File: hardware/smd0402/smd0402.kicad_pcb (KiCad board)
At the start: 2 copper layers, 140 x 40 mm, 79 parts, among them J1 Conn_01x03, J2 Conn_01x03, T1 TestPoint_THTPad_3.0x3.0mm_Dr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, T12 TestPoint_THTPad_3.0x3.0mm_Dr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, T13 TestPoint_THTPad_3.0x3.0mm_Dr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, T14 TestPoint_THTPad_3.0x3.0mm_Dr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, T15 TestPoint_THTPad_3.0x3.0mm_Dr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, T16 TestPoint_THTPad_3.0x3.0mm_Dr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, T18 TestPoint_THTPad_3.0x3.0mm_Dr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, T19 TestPoint_THTPad_3.0x3.0mm_Dr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, T20 TestPoint_THTPad_3.0x3.0mm_Dr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, T21 TestPoint_THTPad_3.0x3.0mm_Dr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, T22 TestPoint_THTPad_3.0x3.0mm_Dr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, T42 TestPoint_THTPad_D1.0mm_Drill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, T43 TestPoint_THTPad_D1.0mm_Drill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, T44 TestPoint_THTPad_D1.0mm_Drill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, T45 TestPoint_THTPad_D1.0mm_Drill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, T46 TestPoint_THTPad_D1.0mm_Drill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, T48 TestPoint_THTPad_D1.0mm_Drill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, T49 TestPoint_THTPad_D1.0mm_Drill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, T50 TestPoint_THTPad_D1.0mm_Drill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, T51 TestPoint_THTPad_D1.0mm_Drill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, T51 TestPoint_THTPad_D2.0mm_Drill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, T52 TestPoint_THTPad_D1.0mm_Drill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, T52 TestPoint_THTPad_D2.0mm_Drill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, T53 TestPoint_THTPad_D2.0mm_Drill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, T54 TestPoint_THTPad_D2.0mm_Drill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, T55 TestPoint_THTPad_D2.0mm_Drill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, T56 TestPoint_THTPad_D2.0mm_Drill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, U1 WCH CH32V003F4U6

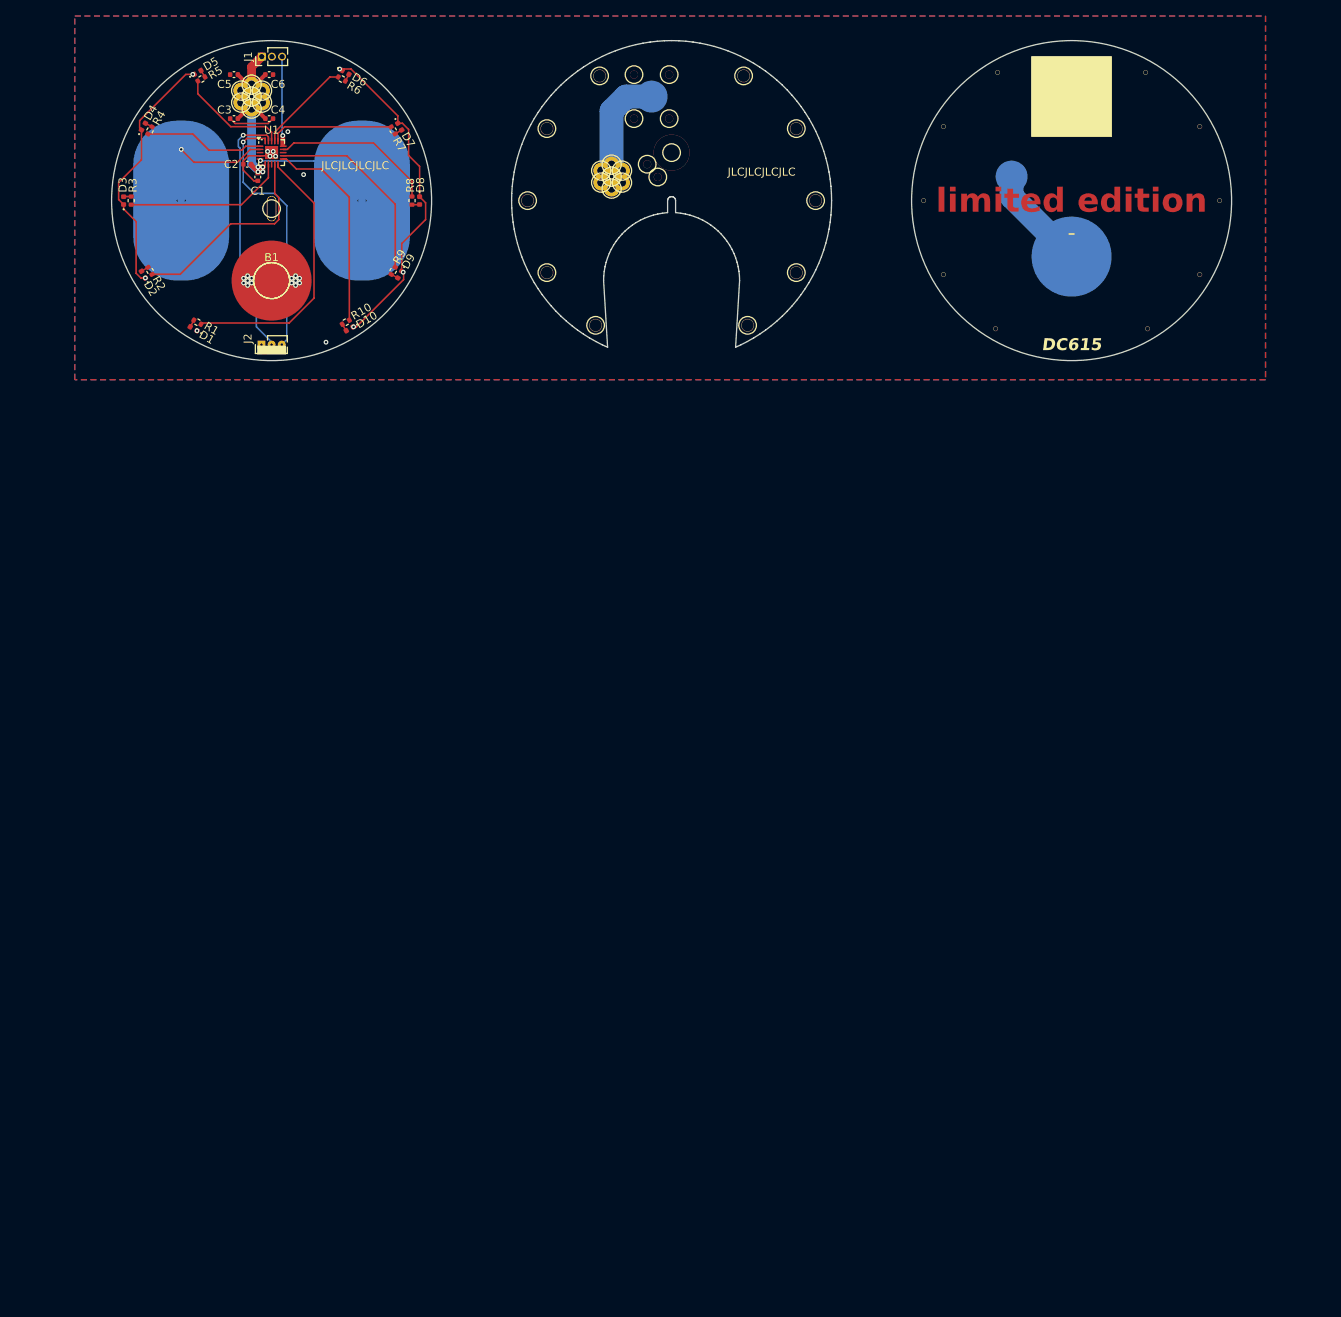
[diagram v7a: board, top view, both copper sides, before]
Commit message: boost dia to 50mm, use back-to-back LEDs, add SAO
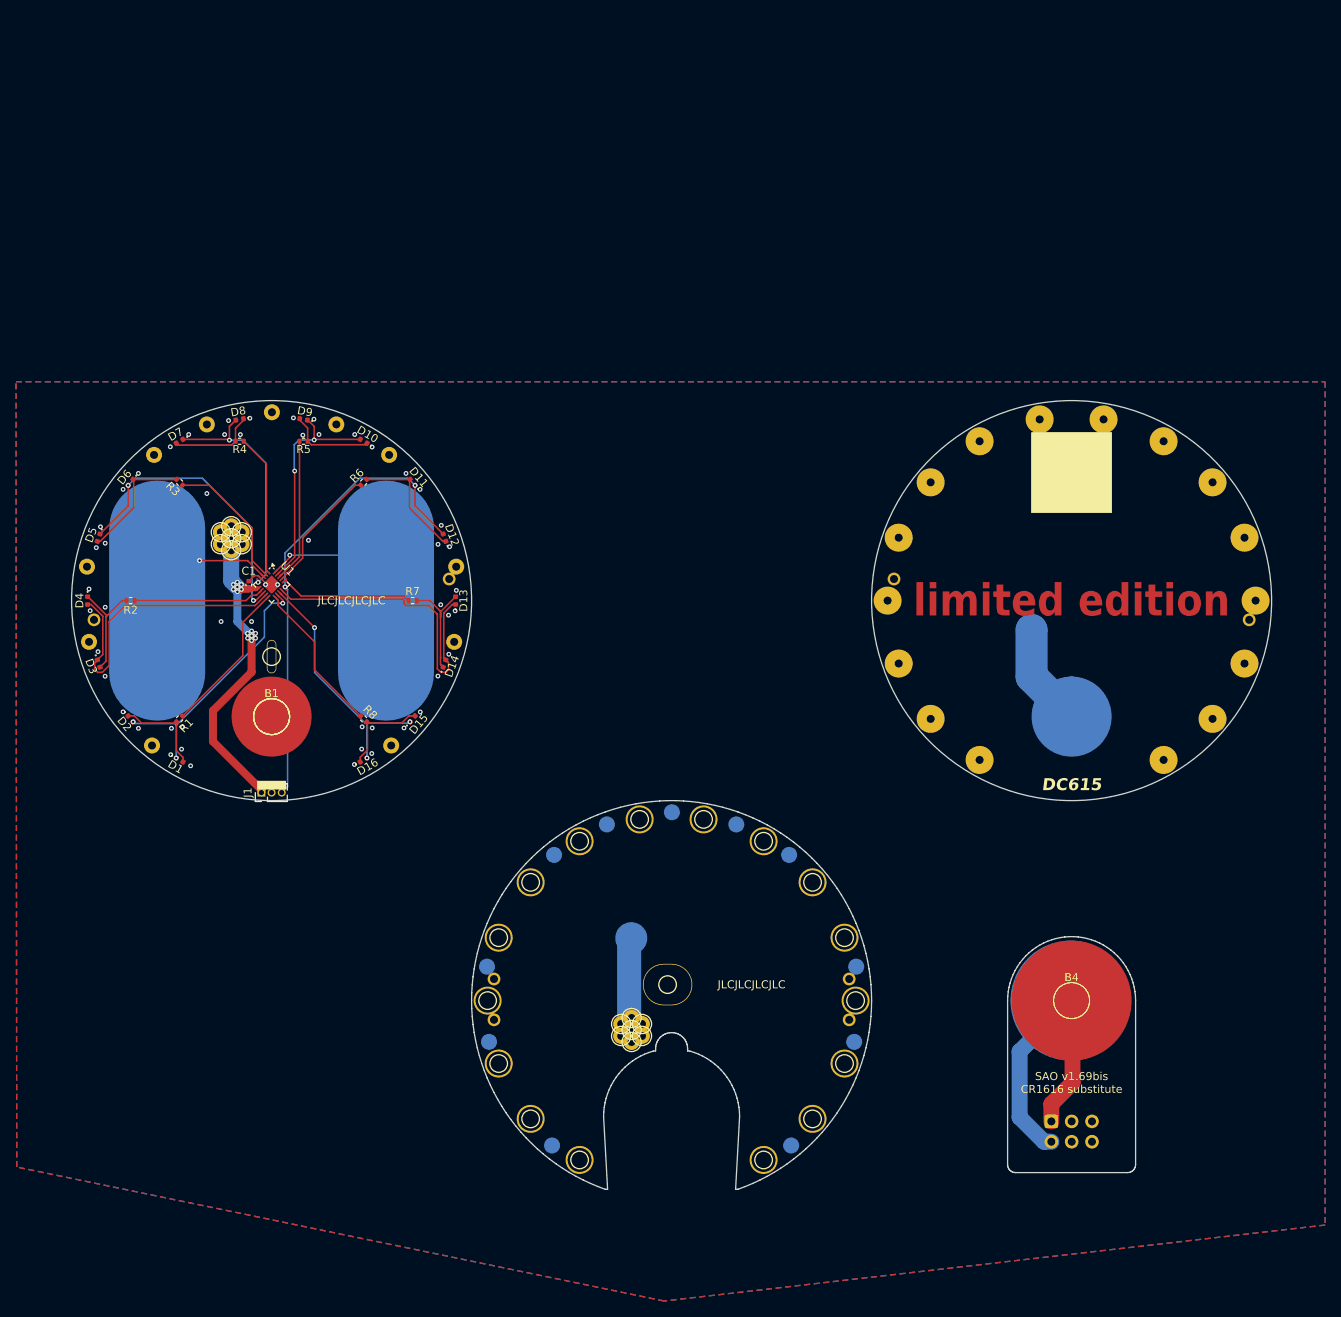
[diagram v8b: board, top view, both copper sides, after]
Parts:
- removed C2, C3, C4, C5, C6: 1u, Capacitor_SMD:C_0402_1005Metric
- removed R10, R9: 47R, Resistor_SMD:R_0402_1005Metric
- removed T12, T13, T14, T15, T16, T18, T19, T20, T21 (x7), T22: TestPoint_THTPad_3.0x3.0mm_Drill1.5mm, TestPoint:TestPoint_THTPad_3.0x3.0mm_Drill1.5mm
- removed T42, T43, T44, T45, T46, T48, T49, T50, T51, T52: TestPoint_THTPad_D1.0mm_Drill0.5mm, TestPoint:TestPoint_THTPad_D1.0mm_Drill0.5mm
- added B3: BAT-, TestPoint:TestPoint_Pad_D4.0mm, B.Cu at (150.0, 150.0)
- added B4: BAT+, TestPoint:TestPoint_Pad_D4.0mm, F.Cu at (150.0, 150.0)
- added D11: LED, LED_SMD:LED_0402_1005Metric, F.Cu at (67.6, 85.2)
- added D12: LED, LED_SMD:LED_0402_1005Metric, F.Cu at (71.6, 92.1)
- added D13: LED, LED_SMD:LED_0402_1005Metric, F.Cu at (73.0, 100.0)
- added D14: LED, LED_SMD:LED_0402_1005Metric, F.Cu at (71.6, 107.9)
- added D15: LED, LED_SMD:LED_0402_1005Metric, F.Cu at (67.6, 114.8)
- added D16: LED, LED_SMD:LED_0402_1005Metric, F.Cu at (61.5, 119.9)
- added SAO-P1, SAO-P2: , , B.Cu at (150.0, 150.0)
- added align-io1: , , F.Cu at (77.8, 147.3)
- added align-io2: , , F.Cu at (122.2, 152.4)
- added align-ir1: , , F.Cu at (77.8, 152.4)
- added align-ir2: , , F.Cu at (122.2, 147.3)
- added align-o1: , , F.Cu at (127.8, 97.3)
- added align-o2: , , F.Cu at (172.2, 102.4)
- added align-r1: , , F.Cu at (27.8, 102.4)
- added align-r2: , , F.Cu at (72.2, 97.3)
- added aperture-D1: TestPoint_THTPad_D1.0mm_Drill0.5mm, TestPoint:TestPoint_THTPad_D1.0mm_Drill0.5mm, F.Cu at (138.5, 119.9)
- added aperture-D10: TestPoint_THTPad_D1.0mm_Drill0.5mm, TestPoint:TestPoint_THTPad_D1.0mm_Drill0.5mm, F.Cu at (161.5, 80.1)
- added aperture-D11: TestPoint_THTPad_D1.0mm_Drill0.5mm, TestPoint:TestPoint_THTPad_D1.0mm_Drill0.5mm, F.Cu at (167.6, 85.2)
- added aperture-D12: TestPoint_THTPad_D1.0mm_Drill0.5mm, TestPoint:TestPoint_THTPad_D1.0mm_Drill0.5mm, F.Cu at (171.6, 92.1)
- added aperture-D13: TestPoint_THTPad_D1.0mm_Drill0.5mm, TestPoint:TestPoint_THTPad_D1.0mm_Drill0.5mm, F.Cu at (173.0, 100.0)
- added aperture-D14: TestPoint_THTPad_D1.0mm_Drill0.5mm, TestPoint:TestPoint_THTPad_D1.0mm_Drill0.5mm, F.Cu at (171.6, 107.9)
- added aperture-D15: TestPoint_THTPad_D1.0mm_Drill0.5mm, TestPoint:TestPoint_THTPad_D1.0mm_Drill0.5mm, F.Cu at (167.6, 114.8)
- added aperture-D16: TestPoint_THTPad_D1.0mm_Drill0.5mm, TestPoint:TestPoint_THTPad_D1.0mm_Drill0.5mm, F.Cu at (161.5, 119.9)
- added aperture-D2: TestPoint_THTPad_D1.0mm_Drill0.5mm, TestPoint:TestPoint_THTPad_D1.0mm_Drill0.5mm, F.Cu at (132.4, 114.8)
- added aperture-D3: TestPoint_THTPad_D1.0mm_Drill0.5mm, TestPoint:TestPoint_THTPad_D1.0mm_Drill0.5mm, F.Cu at (128.4, 107.9)
- added aperture-D4: TestPoint_THTPad_D1.0mm_Drill0.5mm, TestPoint:TestPoint_THTPad_D1.0mm_Drill0.5mm, F.Cu at (127.0, 100.0)
- added aperture-D5: TestPoint_THTPad_D1.0mm_Drill0.5mm, TestPoint:TestPoint_THTPad_D1.0mm_Drill0.5mm, F.Cu at (128.4, 92.1)
- added aperture-D6: TestPoint_THTPad_D1.0mm_Drill0.5mm, TestPoint:TestPoint_THTPad_D1.0mm_Drill0.5mm, F.Cu at (132.4, 85.2)
- added aperture-D7: TestPoint_THTPad_D1.0mm_Drill0.5mm, TestPoint:TestPoint_THTPad_D1.0mm_Drill0.5mm, F.Cu at (138.5, 80.1)
- added aperture-D8: TestPoint_THTPad_D1.0mm_Drill0.5mm, TestPoint:TestPoint_THTPad_D1.0mm_Drill0.5mm, F.Cu at (146.0, 77.3)
- added aperture-D9: TestPoint_THTPad_D1.0mm_Drill0.5mm, TestPoint:TestPoint_THTPad_D1.0mm_Drill0.5mm, F.Cu at (154.0, 77.3)
- added clearance-D1: TestPoint_THTPad_3.0x3.0mm_Drill1.5mm, TestPoint:TestPoint_THTPad_3.0x3.0mm_Drill1.5mm, F.Cu at (88.5, 169.9)
- added clearance-D10: TestPoint_THTPad_3.0x3.0mm_Drill1.5mm, TestPoint:TestPoint_THTPad_3.0x3.0mm_Drill1.5mm, F.Cu at (111.5, 130.1)
- added clearance-D11: TestPoint_THTPad_3.0x3.0mm_Drill1.5mm, TestPoint:TestPoint_THTPad_3.0x3.0mm_Drill1.5mm, F.Cu at (117.6, 135.2)
- added clearance-D12: TestPoint_THTPad_3.0x3.0mm_Drill1.5mm, TestPoint:TestPoint_THTPad_3.0x3.0mm_Drill1.5mm, F.Cu at (121.6, 142.1)
- added clearance-D13: TestPoint_THTPad_3.0x3.0mm_Drill1.5mm, TestPoint:TestPoint_THTPad_3.0x3.0mm_Drill1.5mm, F.Cu at (123.0, 150.0)
- added clearance-D14: TestPoint_THTPad_3.0x3.0mm_Drill1.5mm, TestPoint:TestPoint_THTPad_3.0x3.0mm_Drill1.5mm, F.Cu at (121.6, 157.9)
- added clearance-D15: TestPoint_THTPad_3.0x3.0mm_Drill1.5mm, TestPoint:TestPoint_THTPad_3.0x3.0mm_Drill1.5mm, F.Cu at (117.6, 164.8)
- added clearance-D16: TestPoint_THTPad_3.0x3.0mm_Drill1.5mm, TestPoint:TestPoint_THTPad_3.0x3.0mm_Drill1.5mm, F.Cu at (111.5, 169.9)
- added clearance-D2: TestPoint_THTPad_3.0x3.0mm_Drill1.5mm, TestPoint:TestPoint_THTPad_3.0x3.0mm_Drill1.5mm, F.Cu at (82.4, 164.8)
- added clearance-D3: TestPoint_THTPad_3.0x3.0mm_Drill1.5mm, TestPoint:TestPoint_THTPad_3.0x3.0mm_Drill1.5mm, F.Cu at (78.4, 157.9)
- added clearance-D4: TestPoint_THTPad_3.0x3.0mm_Drill1.5mm, TestPoint:TestPoint_THTPad_3.0x3.0mm_Drill1.5mm, F.Cu at (77.0, 150.0)
- added clearance-D5: TestPoint_THTPad_3.0x3.0mm_Drill1.5mm, TestPoint:TestPoint_THTPad_3.0x3.0mm_Drill1.5mm, F.Cu at (78.4, 142.1)
- added clearance-D6: TestPoint_THTPad_3.0x3.0mm_Drill1.5mm, TestPoint:TestPoint_THTPad_3.0x3.0mm_Drill1.5mm, F.Cu at (82.4, 135.2)
- added clearance-D7: TestPoint_THTPad_3.0x3.0mm_Drill1.5mm, TestPoint:TestPoint_THTPad_3.0x3.0mm_Drill1.5mm, F.Cu at (88.5, 130.1)
- added clearance-D8: TestPoint_THTPad_3.0x3.0mm_Drill1.5mm, TestPoint:TestPoint_THTPad_3.0x3.0mm_Drill1.5mm, F.Cu at (96.0, 127.3)
- added clearance-D9: TestPoint_THTPad_3.0x3.0mm_Drill1.5mm, TestPoint:TestPoint_THTPad_3.0x3.0mm_Drill1.5mm, F.Cu at (104.0, 127.3)
- added stitch1: , , F.Cu at (26.9, 95.8)
- added stitch1: , , F.Cu at (58.1, 78.0)
- added stitch1: , , F.Cu at (50.0, 76.5)
- added stitch1: , , F.Cu at (41.9, 78.0)
- added stitch1: , , F.Cu at (27.2, 105.2)
- added stitch1: , , F.Cu at (35.3, 81.8)
- added stitch1: , , F.Cu at (35.1, 118.1)
- added stitch1: , , F.Cu at (64.9, 118.1)
- added stitch1: , , F.Cu at (73.1, 95.8)
- added stitch1: , , F.Cu at (64.7, 81.8)
- added stitch1: , , F.Cu at (72.8, 105.2)
- added stitch2: TestPoint_Pad_D2.0mm, TestPoint:TestPoint_Pad_D2.0mm, B.Cu at (114.9, 168.1)
- added stitch2: TestPoint_Pad_D2.0mm, TestPoint:TestPoint_Pad_D2.0mm, B.Cu at (77.2, 155.2)
- added stitch2: TestPoint_Pad_D2.0mm, TestPoint:TestPoint_Pad_D2.0mm, B.Cu at (85.1, 168.1)
- added stitch2: TestPoint_Pad_D2.0mm, TestPoint:TestPoint_Pad_D2.0mm, B.Cu at (100.0, 126.5)
- added stitch2: TestPoint_Pad_D2.0mm, TestPoint:TestPoint_Pad_D2.0mm, B.Cu at (122.8, 155.2)
- added stitch2: TestPoint_Pad_D2.0mm, TestPoint:TestPoint_Pad_D2.0mm, B.Cu at (85.3, 131.8)
- added stitch2: TestPoint_Pad_D2.0mm, TestPoint:TestPoint_Pad_D2.0mm, B.Cu at (114.7, 131.8)
- added stitch2: TestPoint_Pad_D2.0mm, TestPoint:TestPoint_Pad_D2.0mm, B.Cu at (91.9, 128.0)
- added stitch2: TestPoint_Pad_D2.0mm, TestPoint:TestPoint_Pad_D2.0mm, B.Cu at (123.1, 145.8)
- added stitch2: TestPoint_Pad_D2.0mm, TestPoint:TestPoint_Pad_D2.0mm, B.Cu at (76.9, 145.8)
- added stitch2: TestPoint_Pad_D2.0mm, TestPoint:TestPoint_Pad_D2.0mm, B.Cu at (108.1, 128.0)
- J2: value Conn_01x03 -> SAO v1.69bis addon; footprint Connector_PinHeader_1.27mm:PinHeader_1x03_P1.27mm_Vertical -> Connector_IDC:IDC-Header_2x03_P2.54mm_Vertical; moved to B.Cu
- moved J2 138.5 mm to (147.5, 165.1), turned to -90 degrees
- moved through-i1 106.7 mm to (95.0, 153.7)
- moved through-i2 106.7 mm to (95.0, 152.2)
- moved through-i3 106.7 mm to (96.3, 152.9)
- moved through-i4 106.7 mm to (96.3, 154.4)
- moved through-i5 106.7 mm to (95.0, 155.2)
- moved through-i6 106.7 mm to (93.7, 154.4)
- moved through-i7 106.7 mm to (93.7, 152.9)
- moved contact-i1 105.2 mm to (95.0, 142.2)
- moved clearance-U1 104.0 mm to (99.5, 148.0)
- moved J1 92.0 mm to (48.7, 124.0)
- moved R8 65.1 mm to (61.5, 114.8), turned to -45 degrees
- moved D4 59.7 mm to (27.0, 100.0), turned to -90 degrees
- moved D5 59.5 mm to (28.4, 92.1), turned to -110 degrees
- moved R7 58.8 mm to (67.6, 100.0), turned to 0 degrees
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- renumbered S2 to S1, S1 to S2, T1 to battery-eject1, T1 to clearance-U1, REF** to contact-i1, REF** to contact-o1, T51 to through-i1, T51 to through-i2, T52 to through-i3, T53 to through-i4, T54 to through-i5, T55 to through-i6, T56 to through-i7, T51 to through-r1, T51 to through-r2, T52 to through-r3, T53 to through-r4, T54 to through-r5, T55 to through-r6, T56 to through-r7
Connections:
- net /LED1 renamed PWM1
- net /LED4 renamed PWM4
- net /LED5 renamed PWM5
- net /LED6 renamed PWM6
- net /LED7 renamed PWM7
- net /SWIO renamed GP6
- D1 pad 1: GND -> GP1
- D10 pad 1: GND -> Net-(D10-K)
- D10 pad 2: Net-(D10-A) -> GP5
- D2 pad 1: GND -> Net-(D1-A)
- D2 pad 2: Net-(D2-A) -> GP1
- D3 pad 1: GND -> GP2
- D4 pad 1: GND -> Net-(D3-A)
- D4 pad 2: Net-(D4-A) -> GP2
- D5 pad 1: GND -> GP3
- D6 pad 1: GND -> Net-(D5-A)
- D6 pad 2: Net-(D6-A) -> GP3
- D7 pad 1: GND -> GP4
- D8 pad 1: GND -> Net-(D7-A)
- D8 pad 2: Net-(D8-A) -> GP4
- D9 pad 1: GND -> GP5
- D9 pad 2: Net-(D9-A) -> Net-(D10-K)
- J2 pad 1: GND -> +3V0
- J2 pad 2: /TX -> GND
- J2 pad 3: /RX -> unconnected-(J2-SDA-Pad3)
- R2 pad 1: /LED2 -> PWM2
- R2 pad 2: Net-(D2-A) -> Net-(D3-A)
- R3 pad 1: /LED3 -> PWM3
- R3 pad 2: Net-(D3-A) -> Net-(D5-A)
- R4 pad 2: Net-(D4-A) -> Net-(D7-A)
- R5 pad 2: Net-(D5-A) -> Net-(D10-K)
- R6 pad 2: Net-(D6-A) -> Net-(D11-A)
- R7 pad 2: Net-(D7-A) -> Net-(D13-A)
- R8 pad 1: /LED8 -> PWM8
- R8 pad 2: Net-(D8-A) -> Net-(D15-A)
- S1 pad 1: /touch2 -> /touch1
- S2 pad 1: /touch1 -> /touch2
- U1 pad 11: /LED10 -> PWM8
- U1 pad 12: /LED9 -> GP1
- U1 pad 13: unconnected-(U1-PC6-Pad13) -> GP8
- U1 pad 14: /LED8 -> GP7
- U1 pad 19: /TX -> GP5
- U1 pad 2: /touch1 -> PWM3
- U1 pad 20: /RX -> /touch1
- U1 pad 21: VSS -> GND
- U1 pad 3: unconnected-(U1-PA2-Pad3) -> /touch2
- U1 pad 5: /touch2 -> GP4
- U1 pad 7: /LED3 -> PWM2
- U1 pad 8: unconnected-(U1-PC1-Pad8) -> GP3
- U1 pad 9: /LED2 -> GP2
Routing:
- net GND: track 87.4 -> 25.4 mm, vias 27 -> 53
- net GP6: track 11.0 -> 58.6 mm, vias 1 -> 2
- net GP7: track 0.00 -> 38.6 mm
- net GP2: track 0.00 -> 38.3 mm
- net GP3: track 0.00 -> 37.0 mm, vias 0 -> 2
- net /RX: track 33.0 -> 0.00 mm, vias 1 -> 0
- net GP1: track 0.00 -> 32.5 mm, vias 0 -> 3
- net /TX: track 32.2 -> 0.00 mm, vias 1 -> 0
- net GP8: track 0.00 -> 30.8 mm, vias 0 -> 3
- net GP4: track 0.00 -> 30.0 mm, vias 0 -> 2
- net GP5: track 0.00 -> 28.5 mm, vias 0 -> 2
- net /LED2: track 25.8 -> 0.00 mm
- net /LED10: track 25.6 -> 0.00 mm
- net /LED9: track 24.4 -> 0.00 mm
- net +3V0: track 59.5 -> 83.5 mm, vias 4 -> 14
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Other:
- board size 140 x 40 mm -> 150 x 98.6 mm
- board text added: "3V"
- board text added: "SAO v1.69bis CR1616 substitute"
- board text added: "SWD"
- board text added: "import QR SVG scale 0.2"
- board text removed: "-"
